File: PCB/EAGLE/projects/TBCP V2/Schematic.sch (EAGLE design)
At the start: 98 parts, among them J1 12 Supply, J2 TB Header, J3 FP Header, Q1 TRANSISTOR-FET_DMP2004K, SW2 SWITCH-SPDT-SMD-RIGHT-ANGLE, U1 ESP32-DEVKITC, U2 TLE9201SG, U3 LM7805_SOT223

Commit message: TBCP 2.0 Board layout half done
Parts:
- removed R16: 100K, rcl:R-EU_R2012
- removed S5: MOMENTARY-SWITCH-SPST-PTH-6.0MM, SparkFun-Switches:MOMENTARY-SWITCH-SPST-PTH-6.0MM
- removed SJ1: JUMPER-SMT_3_1-NC_PASTE_SILK, SparkFun-Jumpers:JUMPER-SMT_3_1-NC_PASTE_SILK
- removed SW2: SWITCH-SPDT-SMD-RIGHT-ANGLE, One_Dimensional_Pong:SWITCH-SPDT-SMD-RIGHT-ANGLE
- removed TP37, TP38, TP39, TP41: TESTPOINT_TPS-SMD-10SN, 52101-101-REV-A_v16:TESTPOINT_TPS-SMD-10SN
- added J4: TB Header, Terminal 5.08 Pitch 6S 1757284:1757284
- added R18: (no value), rcl:R-EU_R2012
- added S1: (no value), SparkFun-Retired:TAC_SWITCHSMD
- added SW1: SWITCH-SPDT-SMD-RIGHT-ANGLE, One_Dimensional_Pong:SWITCH-SPDT-SMD-RIGHT-ANGLE
- added TP58, TP59, TP60, TP61, TP62, TP63, TP68, TP69, TP70, TP71, TP72, TP73, TP74: TESTPOINT_TPS-SMD-10SN, 52101-101-REV-A_v16:TESTPOINT_TPS-SMD-10SN
- added TP76: GPIO34, 52101-101-REV-A_v16:TESTPOINT_TPS-SMD-10SN
- added Z1: MM5Z10VT1G, MM5Z10VT1G:MM5Z10VT1G
- C1, C2: value 0.1uf -> C0805C224J1RACTU; device 1C10X7R104K050B:1C10X7R104K050B -> C0805C224J1RACTU:C0805C224J1RACTU
- D6: value 1N4740A-TR -> 150080AS75000; device Diodes-2:1N4740A-TR -> Wurth_LEDs_WL-SMCW:WL-SMCW_0805_150080AS75000
- J1: value 12 Supply -> ADS1115; device Terminal 5.08 Pitch 2S :1757284 -> ADS1115:ADS1115
- J2: value TB Header -> FP Header
- J3: value FP Header -> 12 Supply; device Terminal 5.08 Pitch 6S 1757284:1757284 -> Terminal 5.08 Pitch 2S :1757284
- Q1: value TRANSISTOR-FET_DMP2004K -> DMP4025LK3Q-13; device 52101-101-REV-A_v16:TRANSISTOR-FET_DMP2004K -> DMP4025LK3Q-13:DMP4025LK3Q-13
- R1, R3, R5: value 5k -> (none); device rcl:R-EU_0207/10 -> rcl:R-EU_R2012
- R10, R12, R14: value (none) -> 8000
- R11, R13, R9: value (none) -> 100k
- R15: value (none) -> 100K
- R17: value 91A1A-B28-B15L -> (none); device Potentiometer_Trimmers:91A1A-B28-B15L -> rcl:R-EU_R2012
- R2, R4, R6: value 3.3k -> (none); device rcl:R-EU_0207/10 -> rcl:R-EU_R2012
- S2, S3, S4: value MOMENTARY-SWITCH-SPST-PTH-6.0MM -> (none); device SparkFun-Switches:MOMENTARY-SWITCH-SPST-PTH-6.0MM -> SparkFun-Retired:TAC_SWITCHSMD
- TP13: value 3V3 -> TESTPOINT_TPS-SMD-10SN
- TP14: value EN -> TESTPOINT_TPS-SMD-10SN
- TP15: value GPIO36 -> TESTPOINT_TPS-SMD-10SN
- TP16: value GPIO39 -> TESTPOINT_TPS-SMD-10SN
- TP17: value GPIO34 -> TESTPOINT_TPS-SMD-10SN
- TP18: value GPIO35 -> TESTPOINT_TPS-SMD-10SN
- TP19: value GPIO32 -> TESTPOINT_TPS-SMD-10SN
- TP33: value TESTPOINT_TPS-SMD-10SN -> 3V3
- TP34: value TESTPOINT_TPS-SMD-10SN -> EN
- TP35: value TESTPOINT_TPS-SMD-10SN -> GPIO36
- TP36: value TESTPOINT_TPS-SMD-10SN -> GPIO39
- TP40: value TESTPOINT_TPS-SMD-10SN -> GPIO35
- TP42: value TESTPOINT_TPS-SMD-10SN -> GPIO32
- U1: value ESP32-DEVKITC -> 7805; device ESP32-DEVKITC:ESP32-DEVKITC -> IC_Power-Management:LM7805_SOT223
- U2: value TLE9201SG -> ESP32-DEVKITC; device TLE9201SG:TLE9201SG -> ESP32-DEVKITC:ESP32-DEVKITC
- U3: value LM7805_SOT223 -> TLE9201SG; device IC_Power-Management:LM7805_SOT223 -> TLE9201SG:TLE9201SG
- renumbered E13 to E2, TP32 to TP75
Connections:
- removed net FB_TB_INV: TP19.TP, U1.IO32
- removed net FP_FB_SCALED: R1.1, R2.2, TP17.TP, TP53.TP, U1.IO34
- removed net LED_SIG1: S3.2
- removed net LED_SIG2: S4.2
- removed net LED_SIG3: S5.2
- removed net N$6: TP37.TP, U1.IO21
- removed net TB_FB_INV_SCALED: R3.1, R4.2, TP52.TP
- removed net TB_FB_SCALED: R5.1, R6.2, SJ1.3, TP51.TP
- removed net TB_FB_SJ: SJ1.2
- removed net TB_SJ: TP18.TP, U1.IO35
- new net ADDR: J1.5, TP5.TP
- new net ADS1115_A0: J1.7, R14.2, R9.1, TP7.TP
- new net ADS1115_A1: J1.8, R12.2, R13.1, TP8.TP
- new net ADS1115_A2: J1.9, R10.2, R11.1, TP9.TP
- new net ADS1115_A4: J1.10, TP10.TP
- new net BNT_SIG1: R1.1, S2.1, S2.2
- new net BNT_SIG2: R3.1, S3.1, S3.2
- new net BNT_SIG3: R2.1, S1.1, S1.2
- new net BNT_SIG4: R5.1, S4.1, S4.2
- new net N$36: Q1.D, SW1.P
- new net N$37: TP42.TP, U2.IO32
- new net N$41: J1.6, TP6.TP
- new net SCL: J1.3, TP12.TP, TP3.TP, U2.IO22
- new net SDA: J1.4, TP15.TP, TP4.TP, U2.IO21
- net 0VDC: now also C1.1, C2.1, D6.-, J2.3, J2.5, J3.2, J4.6, R1.2, R10.1, R12.1, R14.1, R15.1, R2.2, R3.2, R5.2, TP16.TP, TP2.TP, TP30.TP, TP48.TP, TP68.TP, TP71.TP, U1.GND, U2.GND1, U2.GND2, U2.GND3, U3.!CS, U3.SCK, U3.SI, U3.SO; no longer C1.2, C2.2, J2.6, J3.3, J3.5, R12.2, R13.2, R14.2, R15.2, R16.1, R17.3, R2.1, R4.1, R6.1, TP11.TP, TP26.TP, TP38.TP, TP6.TP, TP9.TP, U1.GND1, U1.GND2, U1.GND3, U2.!CS, U2.GND, U2.SCK, U2.SI, U2.SO
- net 12VDC: now also C1.2, TP59.TP, U1.VI, U3.VS, Z1.K; no longer C1.1, D6.C, Q1.D, R7.2, SW2.O, U2.VS, U3.VI
- net 3.3VDC: now also J1.1, R7.2, S1.3, S1.4, S2.3, S2.4, S3.3, S3.4, S4.3, S4.4, TP1.TP, TP33.TP, TP60.TP, U2.3V3, U3.VSO; no longer R17.1, S2.2, TP13.TP, U1.3V3, U2.VSO
- net 5VDC: now also C2.2, J2.1, J2.6, J4.2, R18.2, TP53.TP, TP62.TP, TP63.TP, TP72.TP, U1.VO, U2.EXT_5V; no longer C2.1, J3.1, J3.2, J3.6, R8.2, TP1.TP, TP12.TP, TP7.TP, TP8.TP, U1.EXT_5V, U3.VO
- net FP_FB: now also J2.4, R11.2, TP73.TP; no longer J3.4, R1.2, TP10.TP
- net HBRDIGE_DISABLE: now also TP22.TP, TP56.TP, U2.IO4, U3.DIS; no longer TP44.TP, TP54.TP, U1.IO4, U2.DIS
- net HBRIDGE_DIRECTION: now also TP23.TP, TP61.TP, U2.IO0, U3.DIR; no longer TP45.TP, TP56.TP, U1.IO0, U2.DIR
- net HBRIDGE_PWM: now also TP24.TP, TP57.TP, U2.IO2, U3.PWM; no longer TP46.TP, TP55.TP, U1.IO2, U2.PWM
- net M0+: now also J4.3, TP29.TP, TP58.TP, U3.OUT1; no longer J2.3, TP3.TP, U2.OUT1
- net M0-: now also J4.5, TP55.TP, TP70.TP, U3.OUT2; no longer J2.5, TP5.TP, U2.OUT2
- net N$1: now also J3.1, SW1.S; no longer J1.1, SW2.P
- net N$10: now also TP20.TP, U2.IO17; no longer TP42.TP, U1.IO17
- net N$11: now also TP21.TP, U2.IO16; no longer TP43.TP, U1.IO16
- net N$12: now also D2.+, R4.1; no longer D4.+, R10.1
- net N$13: now also D1.+, R6.1; no longer D5.+, R11.1
- net N$14: now also R6.2, R8.2; no longer R11.2
- net N$15: now also TP25.TP, U2.IO15; no longer TP47.TP, U1.IO15
- net N$16: now also TP26.TP, U2.SD1; no longer TP48.TP, U1.SD1
- net N$17: now also TP27.TP, U2.SD0; no longer TP49.TP, U1.SD0
- net N$18: now also TP28.TP, U2.CLK; no longer TP50.TP, U1.CLK
- net N$19: now also TP34.TP, U2.EN; no longer TP14.TP, U1.EN
- net N$2: now also D5.+; no longer D1.+
- net N$20: now also TP35.TP, U2.SENSOR_VP; no longer TP15.TP, U1.SENSOR_VP
- net N$21: now also TP36.TP, U2.SENSOR_VN; no longer TP16.TP, U1.SENSOR_VN
- net N$22: now also TP74.TP, U2.IO33; no longer TP20.TP, U1.IO33
- net N$23: now also TP43.TP, U2.IO25; no longer TP21.TP, U1.IO25
- net N$24: now also TP44.TP, U2.IO26; no longer TP22.TP, U1.IO26
- net N$25: now also TP45.TP, U2.IO27; no longer TP23.TP, U1.IO27
- net N$26: now also TP46.TP, U2.IO14; no longer TP24.TP, U1.IO14
- net N$27: now also TP47.TP, U2.IO12; no longer TP25.TP, U1.IO12
- net N$28: now also TP49.TP, U2.IO13; no longer TP27.TP, U1.IO13
- net N$29: now also TP50.TP, U2.SD2; no longer TP28.TP, U1.SD2
- net N$3: now also D6.+, R8.1; no longer TP34.TP, U1.IO22
- net N$30: now also TP51.TP, U2.SD3; no longer TP29.TP, U1.SD3
- net N$31: now also TP52.TP, U2.CMD; no longer TP30.TP, U1.CMD
- net N$32: now also R4.2; no longer R10.2
- net N$33: now also R17.2; no longer R9.2
- net N$34: now also TP76.TP, U2.IO34; no longer R12.1, R13.1, R14.1, R15.1, S2.1, S3.1, S4.1, S5.1
- net N$35: now also TP40.TP, U2.IO35; no longer R17.2, SJ1.1, TP57.TP
- net N$4: now also TP13.TP, U2.TXD0; no longer TP35.TP, U1.TXD0
- net N$5: now also TP14.TP, U2.RXD0; no longer TP36.TP, U1.RXD0
- net N$7: now also R15.2, Z1.A; no longer D6.A, R16.2
- net N$8: now also D4.+, R18.1; no longer D2.+, R8.1
- net N$9: now also R17.1; no longer R9.1
- net SPI_CLOCK: now also TP18.TP, U2.IO18; no longer TP40.TP, U1.IO18
- net SPI_CS: now also TP19.TP, U2.IO5; no longer TP41.TP, U1.IO5
- net SPI_MISO: now also TP17.TP, U2.IO19; no longer TP39.TP, U1.IO19
- net SPI_MOSI: now also TP11.TP, U2.IO23; no longer TP33.TP, U1.IO23
- net TB_FB: now also J4.4, R13.2, TP69.TP; no longer J2.4, R5.2, TP4.TP
- net TB_FB_INV: now also J4.1, R9.2, TP54.TP; no longer J2.1, R3.2, TP2.TP
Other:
- note added: "CHECK FOR REPLACEMENT PARTS"
- note added: "SIG2"
- note added: "SIG3"
- note added: "SIG4"
- note removed: "POWER LED"
- moved on the sheet: D1, D2, D3, D4, D5, J2, R1, R10, R11, R12, R13, R14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

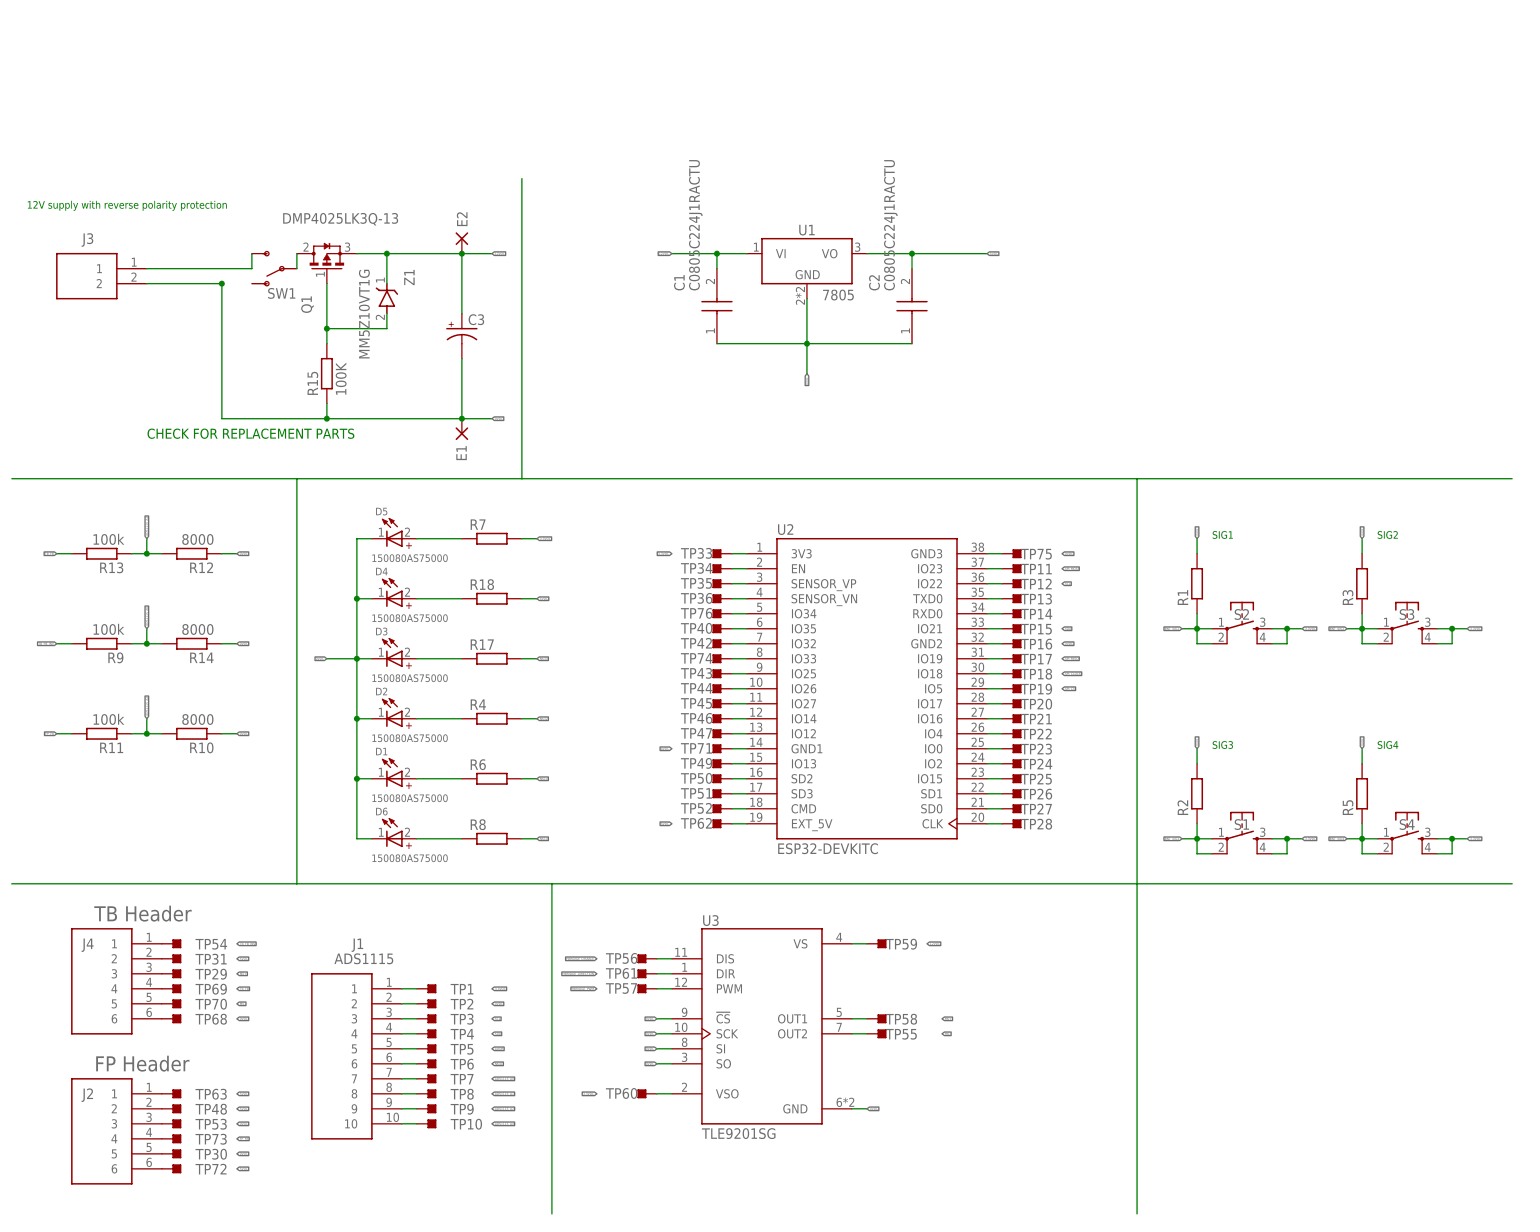
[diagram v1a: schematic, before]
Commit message: Added Serial Studio for TB test
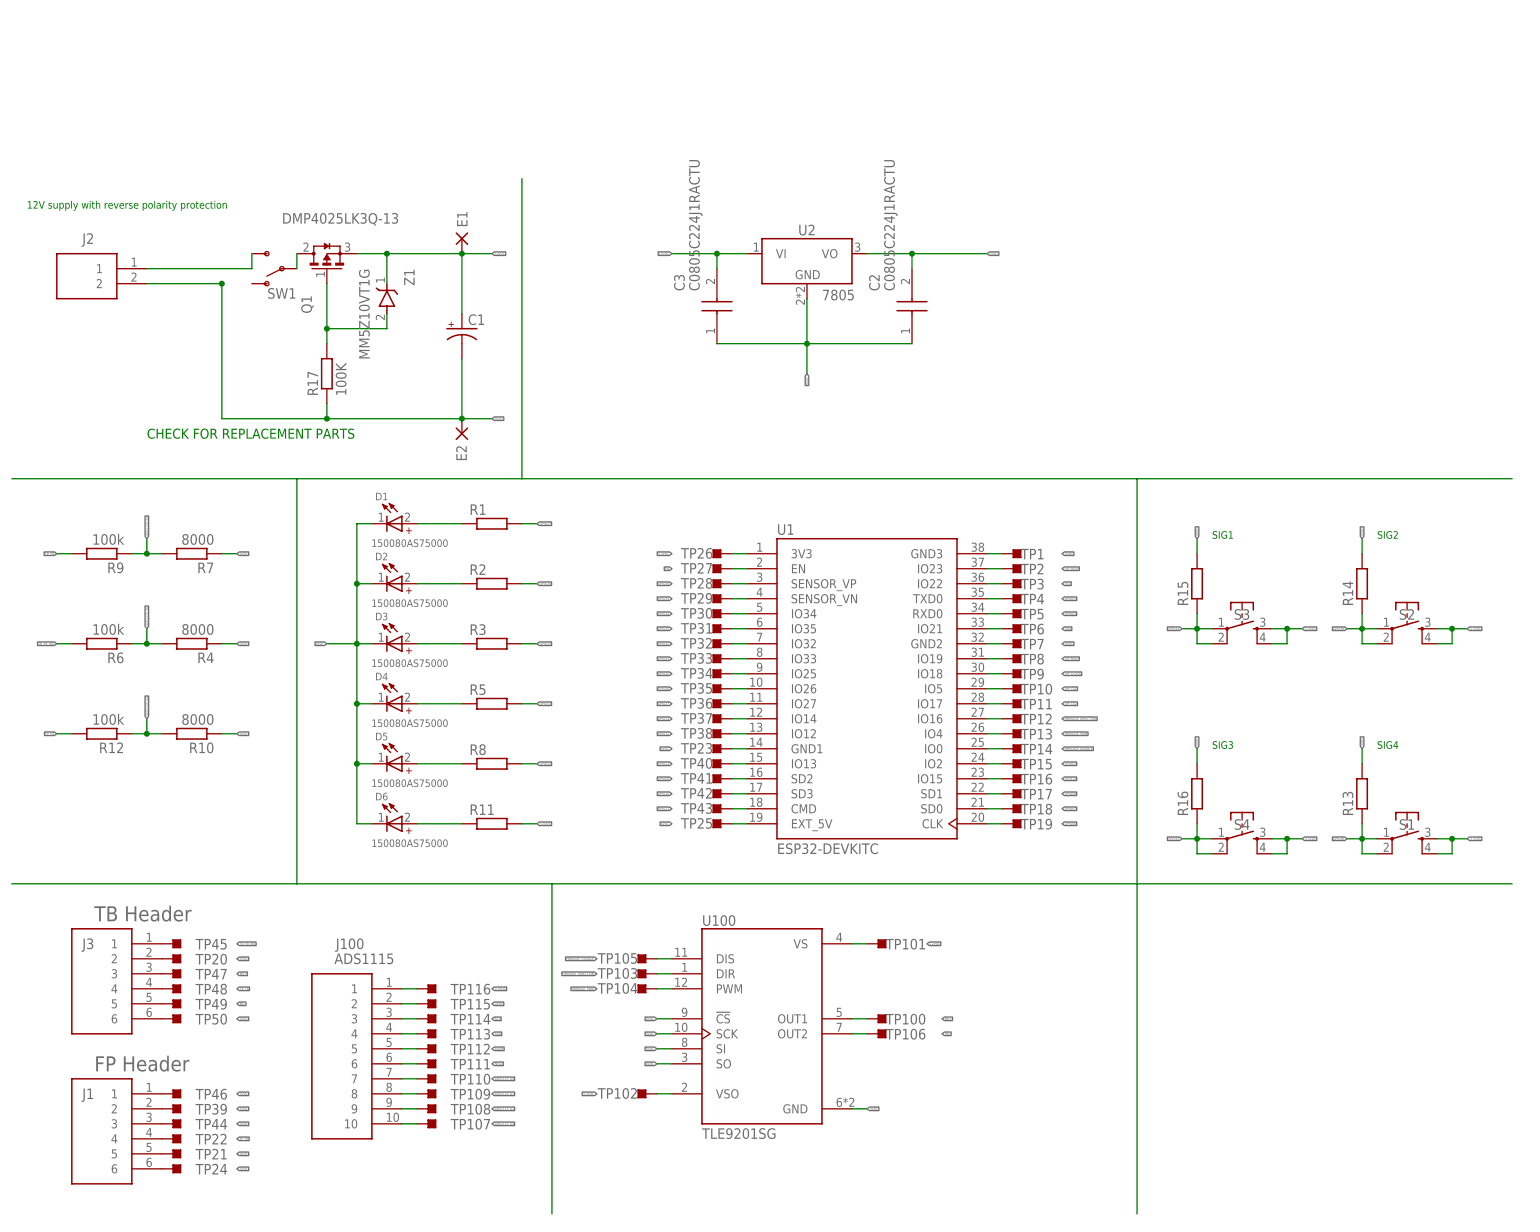
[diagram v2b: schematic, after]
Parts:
- removed J4: TB Header, Terminal 5.08 Pitch 6S 1757284:1757284
- removed R18: (no value), rcl:R-EU_R2012
- removed TP51, TP52, TP53, TP54, TP62, TP63, TP68, TP69, TP70, TP71, TP72, TP73, TP74, TP75: TESTPOINT_TPS-SMD-10SN, 52101-101-REV-A_v16:TESTPOINT_TPS-SMD-10SN
- removed TP76: GPIO34, 52101-101-REV-A_v16:TESTPOINT_TPS-SMD-10SN
- added J100: ADS1115, ADS1115:ADS1115
- added R16: (no value), rcl:R-EU_R2012
- added TP107, TP108, TP109, TP110, TP111, TP112, TP113, TP114, TP115, TP116, TP37, TP38, TP39, TP41: TESTPOINT_TPS-SMD-10SN, 52101-101-REV-A_v16:TESTPOINT_TPS-SMD-10SN
- added TP32: GPIO32, 52101-101-REV-A_v16:TESTPOINT_TPS-SMD-10SN
- C1: value C0805C224J1RACTU -> (none); device C0805C224J1RACTU:C0805C224J1RACTU -> BeagleBone_Blue_R3:CAPACITOR-PE3.5-8
- C3: value (none) -> C0805C224J1RACTU; device BeagleBone_Blue_R3:CAPACITOR-PE3.5-8 -> C0805C224J1RACTU:C0805C224J1RACTU
- J1: value ADS1115 -> FP Header; device ADS1115:ADS1115 -> Terminal 5.08 Pitch 6S 1757284:1757284
- J2: value FP Header -> 12 Supply; device Terminal 5.08 Pitch 6S 1757284:1757284 -> Terminal 5.08 Pitch 2S :1757284
- J3: value 12 Supply -> TB Header; device Terminal 5.08 Pitch 2S :1757284 -> Terminal 5.08 Pitch 6S 1757284:1757284
- R11, R13: value 100k -> (none)
- R12: value 8000 -> 100k
- R14: value 8000 -> (none)
- R15: value 100K -> (none)
- R17: value (none) -> 100K
- R4, R7: value (none) -> 8000
- R6: value (none) -> 100k
- TP26: value TESTPOINT_TPS-SMD-10SN -> 3V3
- TP27: value TESTPOINT_TPS-SMD-10SN -> EN
- TP28: value TESTPOINT_TPS-SMD-10SN -> GPIO36
- TP29: value TESTPOINT_TPS-SMD-10SN -> GPIO39
- TP30: value TESTPOINT_TPS-SMD-10SN -> GPIO34
- TP31: value TESTPOINT_TPS-SMD-10SN -> GPIO35
- TP33: value 3V3 -> TESTPOINT_TPS-SMD-10SN
- TP34: value EN -> TESTPOINT_TPS-SMD-10SN
- TP35: value GPIO36 -> TESTPOINT_TPS-SMD-10SN
- TP36: value GPIO39 -> TESTPOINT_TPS-SMD-10SN
- TP40: value GPIO35 -> TESTPOINT_TPS-SMD-10SN
- TP42: value GPIO32 -> TESTPOINT_TPS-SMD-10SN
- U1: value 7805 -> ESP32-DEVKITC; device IC_Power-Management:LM7805_SOT223 -> ESP32-DEVKITC:ESP32-DEVKITC
- U2: value ESP32-DEVKITC -> 7805; device ESP32-DEVKITC:ESP32-DEVKITC -> IC_Power-Management:LM7805_SOT223
- renumbered TP55 to TP106, TP56 to TP105, TP57 to TP104, TP58 to TP100, TP59 to TP101, TP60 to TP102, TP61 to TP103, U3 to U100
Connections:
- removed net BNT_SIG1: R1.1, S2.1, S2.2
- removed net BNT_SIG2: R3.1, S3.1, S3.2
- removed net BNT_SIG3: R2.1, S1.1, S1.2
- removed net BNT_SIG4: R5.1, S4.1, S4.2
- removed net N$10: TP20.TP, U2.IO17
- removed net N$11: TP21.TP, U2.IO16
- removed net N$14: R6.2, R8.2
- removed net N$15: TP25.TP, U2.IO15
- removed net N$16: TP26.TP, U2.SD1
- removed net N$17: TP27.TP, U2.SD0
- removed net N$18: TP28.TP, U2.CLK
- removed net N$19: TP34.TP, U2.EN
- removed net N$20: TP35.TP, U2.SENSOR_VP
- removed net N$21: TP36.TP, U2.SENSOR_VN
- removed net N$22: TP74.TP, U2.IO33
- removed net N$23: TP43.TP, U2.IO25
- removed net N$24: TP44.TP, U2.IO26
- removed net N$25: TP45.TP, U2.IO27
- removed net N$26: TP46.TP, U2.IO14
- removed net N$27: TP47.TP, U2.IO12
- removed net N$28: TP49.TP, U2.IO13
- removed net N$29: TP50.TP, U2.SD2
- removed net N$30: TP51.TP, U2.SD3
- removed net N$31: TP52.TP, U2.CMD
- removed net N$32: R4.2
- removed net N$33: R17.2
- removed net N$34: TP76.TP, U2.IO34
- removed net N$35: TP40.TP, U2.IO35
- removed net N$37: TP42.TP, U2.IO32
- removed net N$4: TP13.TP, U2.TXD0
- removed net N$5: TP14.TP, U2.RXD0
- removed net SPI_CS: TP19.TP, U2.IO5
- new net EN: TP27.TP, U1.EN
- new net GPIO01: TP4.TP, U1.TXD0
- new net GPIO02: TP15.TP, U1.IO2
- new net GPIO03: TP5.TP, U1.RXD0
- new net GPIO06: TP19.TP, U1.CLK
- new net GPIO07: TP18.TP, U1.SD0
- new net GPIO08: TP17.TP, U1.SD1
- new net GPIO09: TP41.TP, U1.SD2
- new net GPIO10: TP42.TP, U1.SD3
- new net GPIO11: TP43.TP, U1.CMD
- new net GPIO12: TP38.TP, U1.IO12
- new net GPIO13: TP40.TP, U1.IO13
- new net GPIO14: TP37.TP, U1.IO14
- new net GPIO15: TP16.TP, U1.IO15
- new net GPIO25: R3.2, TP34.TP, U1.IO25
- new net GPIO26: R2.2, TP35.TP, U1.IO26
- new net GPIO27: R1.2, TP36.TP, U1.IO27
- new net GPIO32: R8.2, TP32.TP, U1.IO32
- new net GPIO33: R5.2, TP33.TP, U1.IO33
- new net GPIO34: R15.1, S3.1, S3.2, TP30.TP, U1.IO34
- new net GPIO35: R16.1, S4.1, S4.2, TP31.TP, U1.IO35
- new net GPIO36: R13.1, S1.1, S1.2, TP28.TP, U1.SENSOR_VP
- new net GPIO39: R14.1, S2.1, S2.2, TP29.TP, U1.SENSOR_VN
- new net SPI_CS1: TP10.TP, U1.IO5
- new net SPI_CS2: TP11.TP, U1.IO17
- net 0VDC: now also C1.-, C3.1, E2.P, J1.3, J1.5, J100.2, J2.2, J3.6, R13.2, R14.2, R15.2, R16.2, R17.1, R4.1, R7.1, TP1.TP, TP115.TP, TP21.TP, TP23.TP, TP39.TP, TP50.TP, TP7.TP, U1.GND1, U1.GND2, U1.GND3, U2.GND; no longer C1.1, C3.-, E1.P, J1.2, J2.3, J2.5, J3.2, J4.6, R1.2, R12.1, R14.1, R15.1, R2.2, R3.2, R5.2, TP16.TP, TP2.TP, TP30.TP, TP48.TP, TP68.TP, TP71.TP, TP75.TP, U1.GND, U2.GND1, U2.GND2, U2.GND3
- net 12VDC: now also C1.+, C3.2, E1.P, U2.VI; no longer C1.2, C3.+, E2.P, U1.VI
- net 3.3VDC: now also J100.1, R11.2, TP116.TP, TP26.TP, U1.3V3; no longer J1.1, R7.2, TP1.TP, TP33.TP, U2.3V3
- net 5VDC: now also J1.1, J1.2, J1.6, J3.2, TP20.TP, TP24.TP, TP25.TP, TP44.TP, TP46.TP, U1.EXT_5V, U2.VO; no longer J2.1, J2.2, J2.6, J4.2, R18.2, TP31.TP, TP53.TP, TP62.TP, TP63.TP, TP72.TP, U1.VO, U2.EXT_5V
- net ADDR: now also J100.5, TP112.TP; no longer J1.5, TP5.TP
- net ADS1115_A0: now also J100.7, R4.2, R6.1, TP110.TP; no longer J1.7, R14.2, R9.1, TP7.TP
- net ADS1115_A1: now also J100.8, R7.2, R9.1, TP109.TP; no longer J1.8, R12.2, R13.1, TP8.TP
- net ADS1115_A2: now also J100.9, R12.1, TP108.TP; no longer J1.9, R11.1, TP9.TP
- net ADS1115_A4: now also J100.10, TP107.TP; no longer J1.10, TP10.TP
- net FP_FB: now also J1.4, R12.2, TP22.TP; no longer J2.4, R11.2, TP73.TP
- net HBRDIGE_DISABLE: now also TP14.TP, U1.IO0; no longer TP22.TP, U2.IO4
- net HBRIDGE_DIRECTION: now also TP12.TP, U1.IO16; no longer TP23.TP, U2.IO0
- net HBRIDGE_PWM: now also TP13.TP, U1.IO4; no longer TP24.TP, U2.IO2
- net M0+: now also J3.3, TP47.TP; no longer J4.3, TP29.TP
- net M0-: now also J3.5, TP49.TP; no longer J4.5, TP70.TP
- net N$1: now also J2.1; no longer J3.1
- net N$12: now also D4.+, R5.1; no longer D2.+, R4.1
- net N$13: now also D5.+, R8.1; no longer D1.+, R6.1
- net N$2: now also D6.+, R11.1; no longer D5.+, R7.1
- net N$3: now also D1.+, R1.1; no longer D6.+, R8.1
- net N$41: now also J100.6, TP111.TP; no longer J1.6, TP6.TP
- net N$7: now also R17.2; no longer R15.2
- net N$8: now also D2.+, R2.1; no longer D4.+, R18.1
- net N$9: now also R3.1; no longer R17.1
- net SCL: now also J100.3, TP114.TP, U1.IO22; no longer J1.3, TP12.TP, U2.IO22
- net SDA: now also J100.4, TP113.TP, TP6.TP, U1.IO21; no longer J1.4, TP15.TP, TP4.TP, U2.IO21
- net SPI_CLOCK: now also TP9.TP, U1.IO18; no longer TP18.TP, U2.IO18
- net SPI_MISO: now also TP8.TP, U1.IO19; no longer TP17.TP, U2.IO19
- net SPI_MOSI: now also TP2.TP, U1.IO23; no longer TP11.TP, U2.IO23
- net TB_FB: now also J3.4, R9.2, TP48.TP; no longer J4.4, R13.2, TP69.TP
- net TB_FB_INV: now also J3.1, R6.2, TP45.TP; no longer J4.1, R9.2, TP54.TP
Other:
- moved on the sheet: D1, D2, D3, D4, D5, D6, E1, E2, R1, R11, R12, R13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
